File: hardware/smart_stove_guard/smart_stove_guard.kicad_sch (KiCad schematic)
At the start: 10 parts, among them IC1 BS412, SW1 Omron B3F-1000, U1 MLX90614ESF-AAA-000-TU, U3 ESP32-C6-MINI-1, U5 LM1117MP-3.3

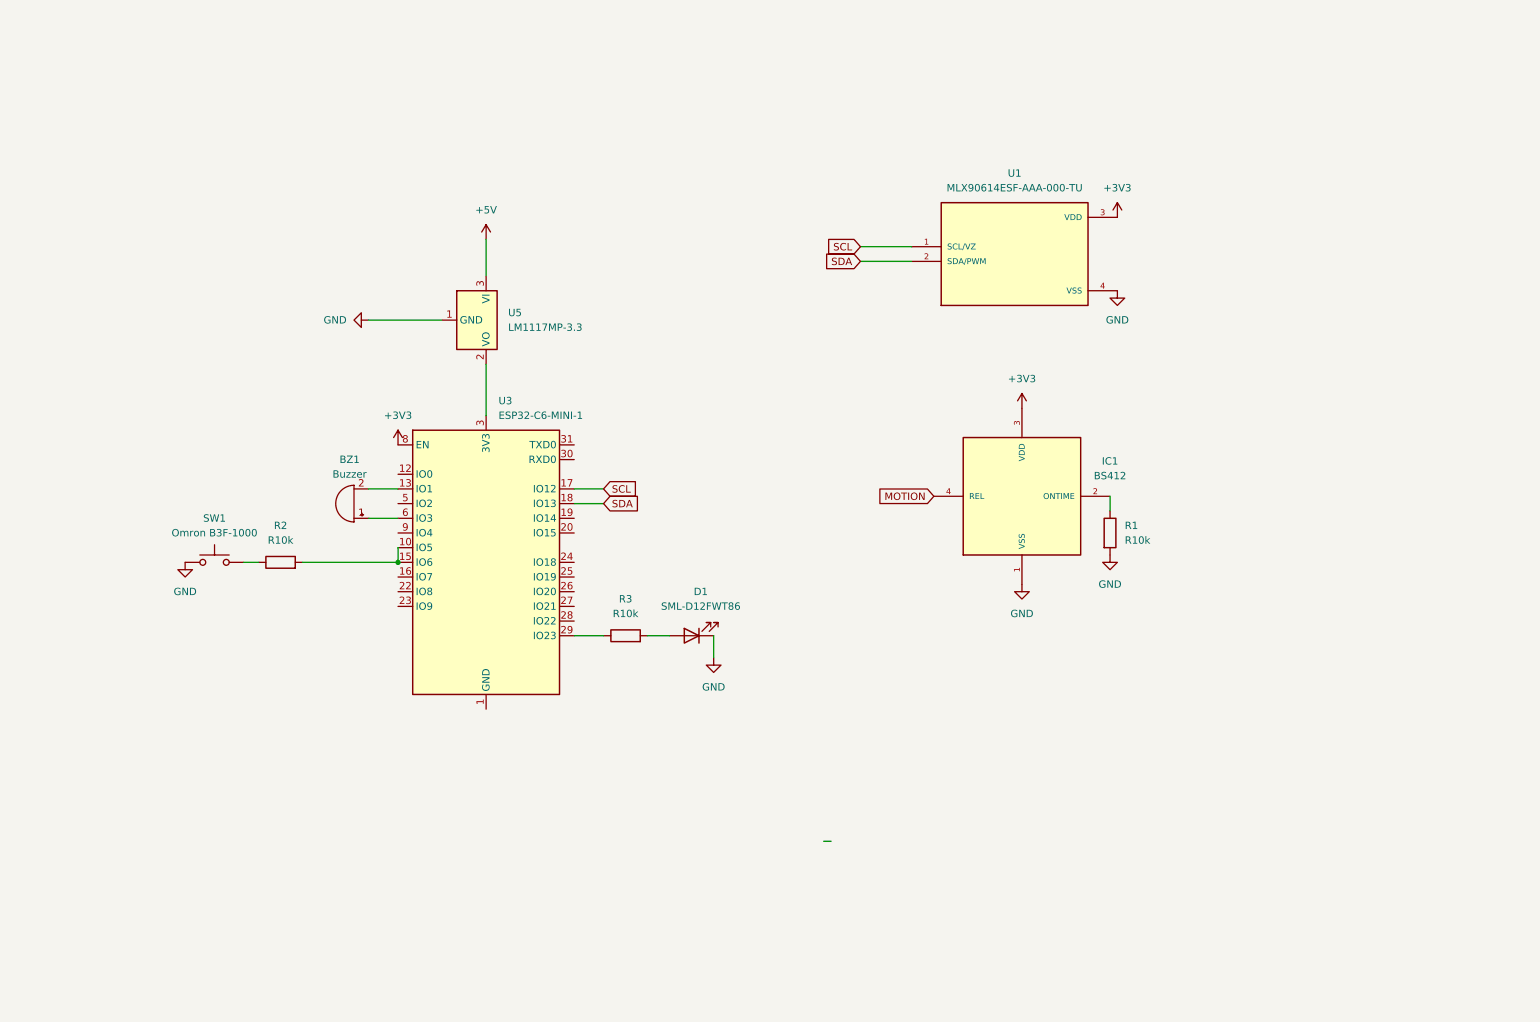
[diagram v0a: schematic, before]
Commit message: Getting schematic ready for pcb + some code changes
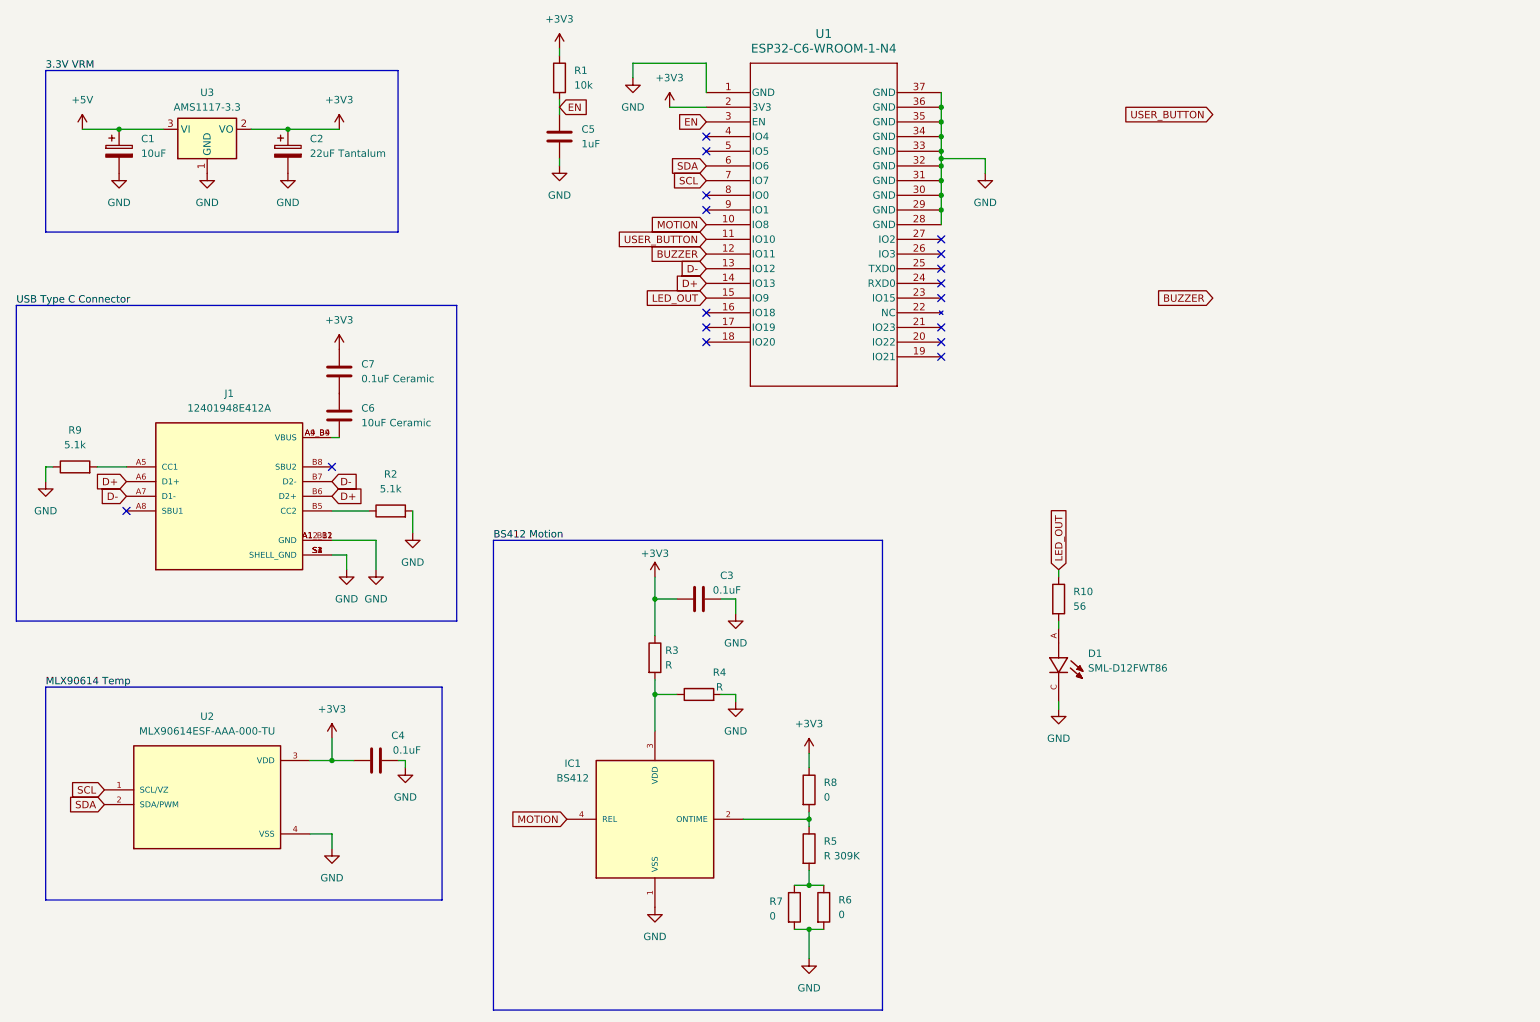
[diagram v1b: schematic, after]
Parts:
- removed BZ1: Buzzer, symbol Device:Buzzer
- removed D1: SML-D12FWT86, Diode_SMD:D_0201_0603Metric, symbol Device:LED
- removed SW1: Omron B3F-1000, symbol Switch:SW_Omron_B3FS
- removed U1: MLX90614ESF-AAA-000-TU, MLX90614ESF-AAA-000-TU:TO254P912H435-4, symbol MLX90614ESF-AAA-000-TU:MLX90614ESF-AAA-000-TU
- removed U3: ESP32-C6-MINI-1, RF_Module:ESP32-C6-MINI-1, symbol RF_Module:ESP32-C6-MINI-1
- removed U5: LM1117MP-3.3, Package_TO_SOT_SMD:SOT-223-3_TabPin2, symbol Regulator_Linear:LM1117MP-3.3
- added C1: 10uF, Capacitor_SMD:C_0805_2012Metric, symbol Device:C_Polarized
- added C2: 22uF Tantalum, Capacitor_SMD:C_0805_2012Metric, symbol Device:C_Polarized
- added C3, C4: 0.1uF, symbol Device:C
- added C5: 1uF, symbol Device:C
- added C6: 10uF Ceramic, symbol Device:C
- added C7: 0.1uF Ceramic, symbol Device:C
- added D1: SML-D12FWT86, SML-D12FWT86:LED_SML-D12FWT86, symbol SML-D12FWT86:SML-D12FWT86
- added J1: 12401948E412A, 12401948E412A:AMPHENOL_12401948E412A, symbol 12401948E412A:12401948E412A
- added R10: 56, symbol Device:R
- added R4: R, symbol Device:R
- added R5: R 309K, symbol Device:R
- added R6, R7, R8: 0, symbol Device:R
- added R9: 5.1k, symbol Device:R
- added U1: ESP32-C6-WROOM-1-N4, MOD28_ESP32-C6-WROOM-1_EXP, symbol esp32-c6-wroom-1-n4:ESP32-C6-WROOM-1-N4
- added U2: MLX90614ESF-AAA-000-TU, MLX90614ESF-AAA-000-TU:TO254P912H435-4, symbol MLX90614ESF-AAA-000-TU:MLX90614ESF-AAA-000-TU
- added U3: AMS1117-3.3, Package_TO_SOT_SMD:SOT-223-3_TabPin2, symbol Regulator_Linear:AMS1117-3.3
- R1: value R10k -> 10k; footprint Resistor_SMD:R_0805_2012Metric -> (none)
- R2: value R10k -> 5.1k
- R3: value R10k -> R
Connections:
- net +3V3: now also R1.1, R3.1, C2.1, C3.2, C4.2, C7.1, R8.1, U1.2 (3V3), U2.3 (VDD), U3.2 (VO); no longer IC1.3 (VDD)
- net +5V: now also C1.1, U3.3 (VI)
- net GND: now also R2.2, C1.2, C2.2, C3.1, C4.1, C5.2, D1.C, J1.A12_B1 (GND), J1.A1_B12 (GND), J1.S1 (SHELL_GND), J1.S2 (SHELL_GND), J1.S3 (SHELL_GND), J1.S4 (SHELL_GND), R4.2, R6.2, R7.2, R9.1, U1.1 (GND), U1.28 (GND), U1.29 (GND), U1.30 (GND), U1.31 (GND), U1.32 (GND), U1.33 (GND), U1.34 (GND), U1.35 (GND), U1.36 (GND), U1.37 (GND), U2.4 (VSS), U3.1 (GND); no longer R1.2
- net MOTION: now also U1.10 (IO8)
- net SCL: now also U1.7 (IO7), U2.1 (SCL/VZ)
- net SDA: now also U1.6 (IO6), U2.2 (SDA/PWM)
- net at IC1.2 (ONTIME): now also R5.1, R8.2; no longer R1.1
- net at R2.1: now also J1.B5 (CC2)
- net at R3.2: now also IC1.3 (VDD), R4.1
- new net: C6.1, C7.2
- new net: C6.2, J1.A4_B9 (VBUS), J1.A9_B4 (VBUS)
- new net: J1.A5 (CC1), R9.2
- new net: R5.2, R6.1, R7.1
- new net: D1.A, R10.2
- new net BUZZER: U1.12 (IO11)
- new net D+: J1.A6 (D1+), J1.B6 (D2+), U1.14 (IO13)
- new net D-: J1.A7 (D1-), J1.B7 (D2-), U1.13 (IO12)
- new net EN: C5.1, R1.2, U1.3 (EN)
- new net LED_OUT: R10.1, U1.15 (IO9)
- new net USER_BUTTON: U1.11 (IO10)
- no-connect marks 0 -> 17

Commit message: Finished initial schematic, added footprints and symbols for missing components
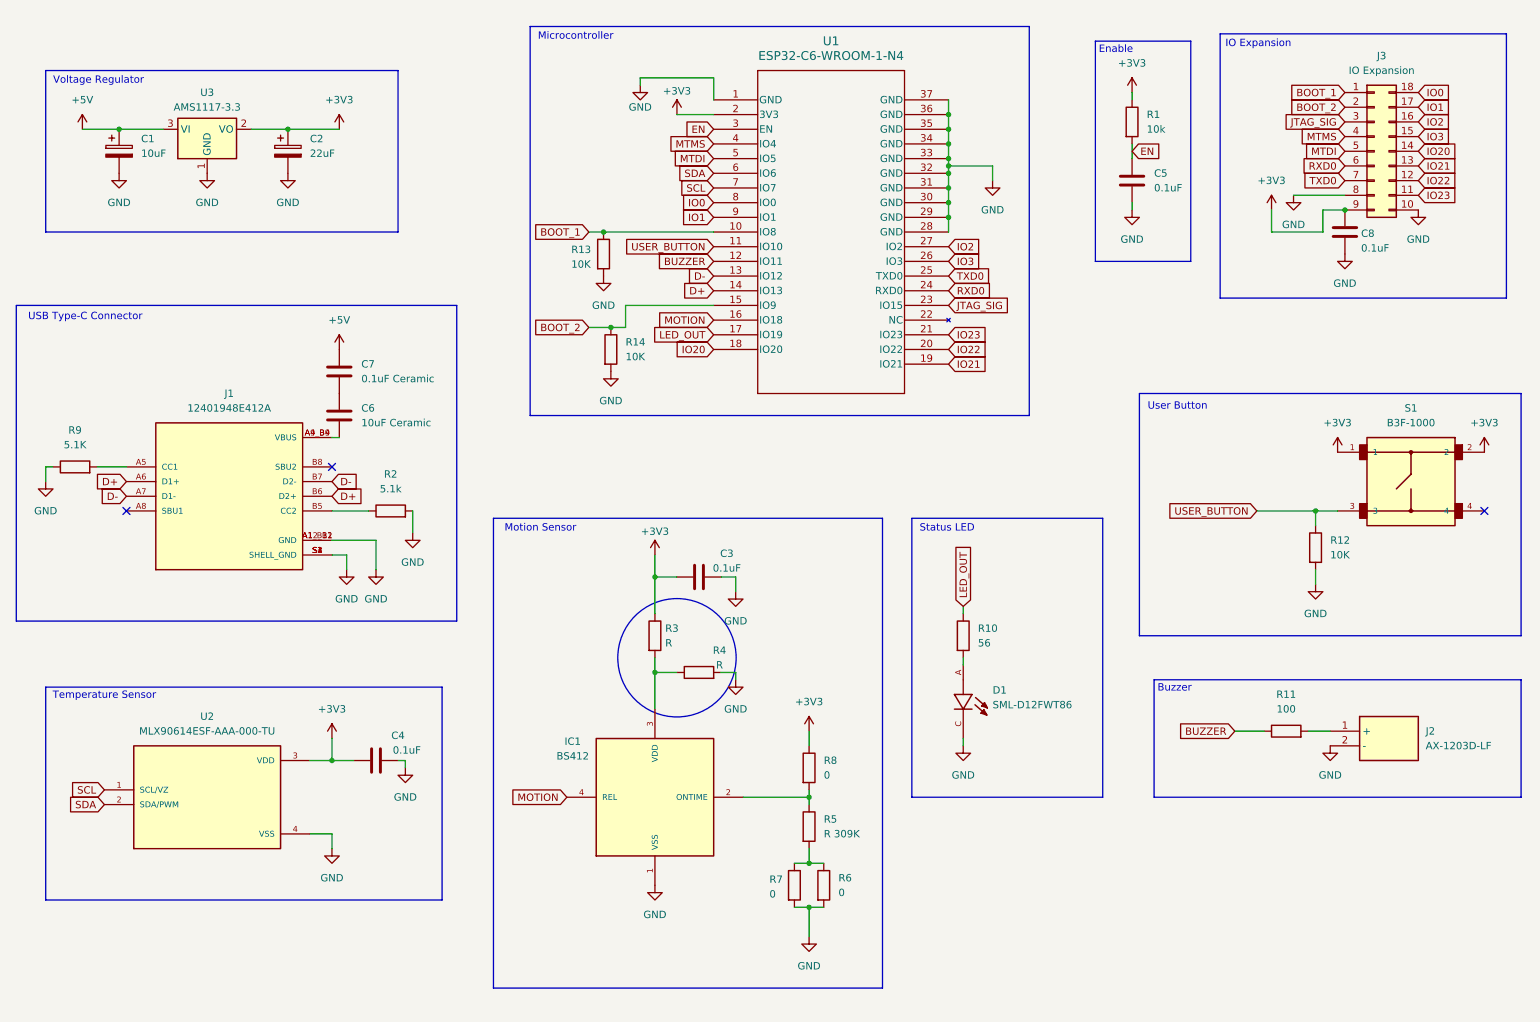
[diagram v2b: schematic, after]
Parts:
- added C8: 0.1uF, Capacitor_SMD:C_0805_2012Metric, symbol Device:C
- added J2: AX-1203D-LF, AX1203DLF, symbol AX-1203D-LF:AX-1203D-LF
- added J3: IO Expansion, Connector_PinSocket_2.54mm:PinSocket_2x09_P2.54mm_Vertical, symbol Connector_Generic:Conn_02x09_Counter_Clockwise
- added R11: 100, Resistor_SMD:R_0805_2012Metric, symbol Device:R
- added R12, R13, R14: 10K, Resistor_SMD:R_0805_2012Metric, symbol Device:R
- added S1: B3F-1000, footprints:SW_B3F-1000, symbol B3F-1000:B3F-1000
- C1: footprint Capacitor_SMD:C_0805_2012Metric -> Capacitor_Tantalum_SMD:CP_EIA-7343-31_Kemet-D_HandSolder
- C2: value 22uF Tantalum -> 22uF; footprint Capacitor_SMD:C_0805_2012Metric -> Capacitor_Tantalum_SMD:CP_EIA-7343-31_Kemet-D_HandSolder
- C3, C4, C6, C7: footprint (none) -> Capacitor_SMD:C_0805_2012Metric
- C5: value 1uF -> 0.1uF; footprint (none) -> Capacitor_SMD:C_0805_2012Metric
- IC1: footprint BS412:BS412 -> footprints:BS412
- J1: footprint 12401948E412A:AMPHENOL_12401948E412A -> footprints:AMPHENOL_12401948E412A
- R10, R2, R3, R4, R5, R6, R7, R8: footprint (none) -> Resistor_SMD:R_0805_2012Metric
- R9: value 5.1k -> 5.1K; footprint (none) -> Resistor_SMD:R_0805_2012Metric
- U2: footprint MLX90614ESF-AAA-000-TU:TO254P912H435-4 -> footprints:MLX90614ESF-AAA-000
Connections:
- net +3V3: now also C8.1, J3.9 (Pin_9), S1.1, S1.2; no longer C7.1
- net +5V: now also C7.1
- net BUZZER: now also R11.1
- net GND: now also C8.2, J2.2 (-), J3.10 (Pin_10), J3.8 (Pin_8), R12.2, R13.2, R14.2
- net LED_OUT: now also U1.17 (IO19); no longer U1.15 (IO9)
- net MOTION: now also U1.16 (IO18); no longer U1.10 (IO8)
- net USER_BUTTON: now also R12.1, S1.3
- net IO20: now reaches U1.18 (IO20)
- net IO20: now also J3.14 (Pin_14)
- net IO21: now reaches U1.19 (IO21)
- net IO21: now also J3.13 (Pin_13)
- net IO22: now reaches U1.20 (IO22)
- net IO22: now also J3.12 (Pin_12)
- net IO23: now reaches U1.21 (IO23)
- net IO23: now also J3.11 (Pin_11)
- net JTAG_SIG: now reaches U1.23 (IO15)
- net JTAG_SIG: now also J3.3 (Pin_3)
- net RXD0: now reaches U1.24 (RXD0)
- net RXD0: now also J3.6 (Pin_6)
- net TXD0: now reaches U1.25 (TXD0)
- net TXD0: now also J3.7 (Pin_7)
- net IO3: now reaches U1.26 (IO3)
- net IO3: now also J3.15 (Pin_15)
- net IO2: now reaches U1.27 (IO2)
- net IO2: now also J3.16 (Pin_16)
- net MTMS: now reaches U1.4 (IO4)
- net MTMS: now also J3.4 (Pin_4)
- net MTDI: now reaches U1.5 (IO5)
- net MTDI: now also J3.5 (Pin_5)
- net IO0: now reaches U1.8 (IO0)
- net IO0: now also J3.18 (Pin_18)
- net IO1: now reaches U1.9 (IO1)
- net IO1: now also J3.17 (Pin_17)
- new net: J2.1 (+), R11.2
- new net BOOT_1: J3.1 (Pin_1), R13.1, U1.10 (IO8)
- new net BOOT_2: J3.2 (Pin_2), R14.1, U1.15 (IO9)
- no-connect marks 17 -> 3
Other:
- note added: "Buzzer"
- note added: "Enable"
- note added: "IO Expansion"
- note added: "Microcontroller"
- note added: "Motion Sensor"
- note added: "Status LED"
- note added: "Temperature Sensor"
- note added: "USB Type-C Connector"
- note added: "User Button"
- note added: "Voltage Regulator"
- moved on the sheet: C3, C5, D1, IC1, R1, R10, R3, R4, R5, R6, R7, R8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

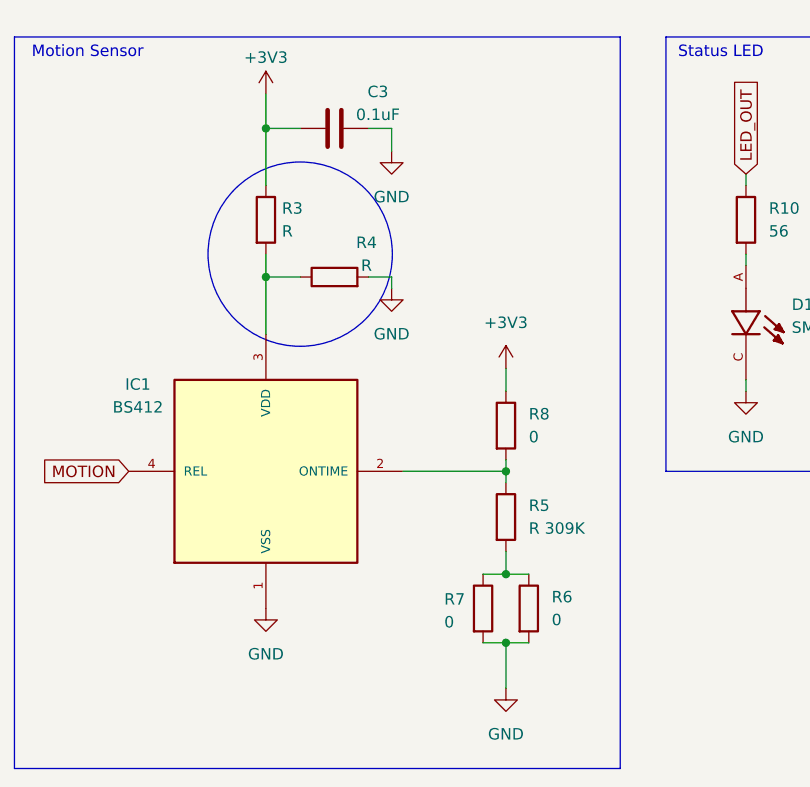
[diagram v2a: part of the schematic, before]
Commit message: Finished Schematic, going to send to TA for look over
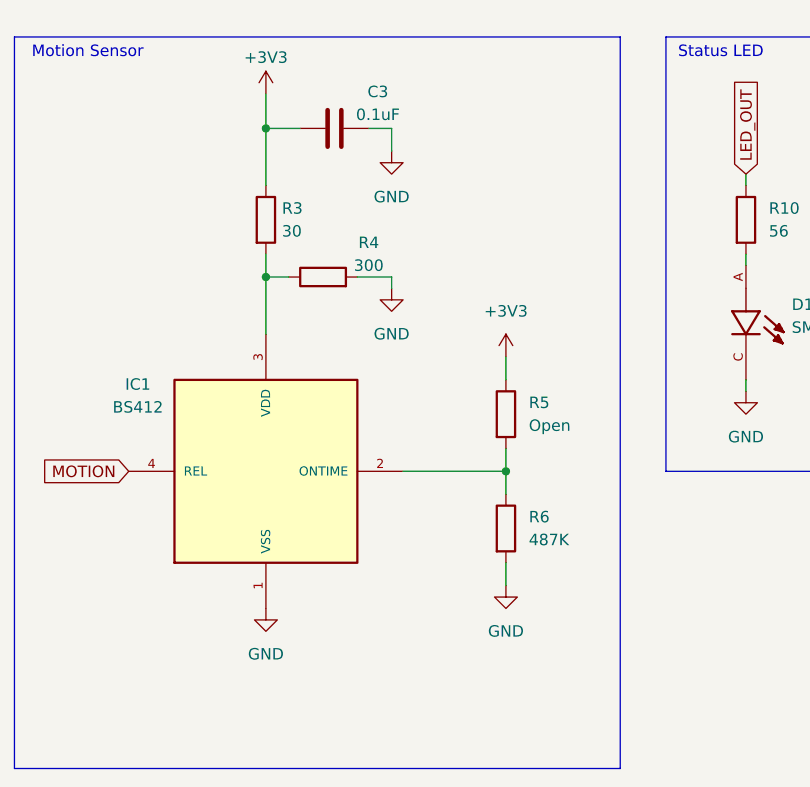
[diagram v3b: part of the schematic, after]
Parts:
- removed R7, R8: 0, Resistor_SMD:R_0805_2012Metric, symbol Device:R
- R3: value R -> 30
- R4: value R -> 300
- R5: value R 309K -> Open; footprint Resistor_SMD:R_0805_2012Metric -> (none)
- R6: value 0 -> 487K; footprint Resistor_SMD:R_0805_2012Metric -> (none)
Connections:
- net +3V3: now also R5.1
- net at IC1.2 (ONTIME): now also R5.2, R6.1; no longer R5.1
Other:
- moved on the sheet: R4

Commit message: Updated footprints
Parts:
- D1: footprint SML-D12FWT86:LED_SML-D12FWT86 -> smart_stove footprints:LED_SML-D12FWT86
- J2: footprint AX1203DLF -> footprints:AX1203DLF
- R1, R5, R6: footprint (none) -> Resistor_SMD:R_0805_2012Metric
- U1: footprint MOD28_ESP32-C6-WROOM-1_EXP -> footprints:MOD28_ESP32-C6-WROOM-1_EXP
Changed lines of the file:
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@@
 			)
 		)
-		(property "Footprint" ""
+		(property "Footprint" "Resistor_SMD:R_0805_2012Metric"
 			(at 155.702 165.1 90)
 			(effects
@@
 			)
 		)
-		(property "Footprint" "AX1203DLF"
+		(property "Footprint" "footprints:AX1203DLF"
 			(at 264.16 242.24 0)
 			(effects
@@
 			)
 		)
-		(property "Footprint" ""
+		(property "Footprint" "Resistor_SMD:R_0805_2012Metric"
 			(at 211.582 41.91 90)
 			(effects
@@
 			)
 		)
-		(property "Footprint" "SML-D12FWT86:LED_SML-D12FWT86"
+		(property "Footprint" "smart_stove footprints:LED_SML-D12FWT86"
 			(at 184.15 143.51 0)
 			(effects
@@
 			)
 		)
-		(property "Footprint" "MOD28_ESP32-C6-WROOM-1_EXP"
+		(property "Footprint" "footprints:MOD28_ESP32-C6-WROOM-1_EXP"
 			(at 140.97 38.1 0)
 			(effects
@@
 			)
 		)
-		(property "Footprint" ""
+		(property "Footprint" "Resistor_SMD:R_0805_2012Metric"
 			(at 155.702 152.4 90)
 			(effects
